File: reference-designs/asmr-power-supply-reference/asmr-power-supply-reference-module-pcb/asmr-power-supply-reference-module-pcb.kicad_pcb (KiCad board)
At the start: 2 copper layers, 136 x 72 mm, 74 parts, among them J2 USB_C_Receptacle_USB2.0_14P, J3 PWR-SW, Q1 DMP3036SFV, U1 HUSB238, U2 MP2328C, U3 MCP1365, U4 MP2328C

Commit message: More changes to DreamLand.
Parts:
- Q1: footprint Package_SON:VSON-8_3.3x3.3mm_P0.65mm_NexFET -> CM_Chip_Packages:VSON-8_3.3x3.3mm_P0.65mm_NexFET
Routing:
- net +20V: track 58.4 -> 53.3 mm

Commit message: Tune final power supply design.
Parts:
- J3: footprint Connector_JST:JST_SH_BM02B-SRSS-TB_1x02-1MP_P1.00mm_Vertical -> CM_Connector_JST:JST_SH_BM02B-SRSS-TB_1x02-1MP_P1.00mm_Vertical
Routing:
- net Net-(J3-Pin_2): track 9.48 -> 10.2 mm
- net GND_CH: vias 298 -> 299
- net /Vbus: vias 0 -> 1
- net -15V: vias 6 -> 7
- net +5V: vias 6 -> 7
- net +20V: vias 4 -> 5
- net +15V: vias 6 -> 7
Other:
- outline, holes or cut-outs redrawn
- board text added: "ABSOLUTELY"
- board text added: "ASMR"
- board text added: "Advanced Synth Module Rack"
- board text added: "Do NOT attempt to use in a computer."
- board text added: "NOT PCI !"
- board text added: "Power Switch"
- board text added: "Reference Power Supply"
- board text added: "Rev. A (2025/09)"
- board text added: "SMOKE, FIRE OR SMELLS MAY OCCUR."
- board text added: "by Circuit Monkey"
- board text added: "for"

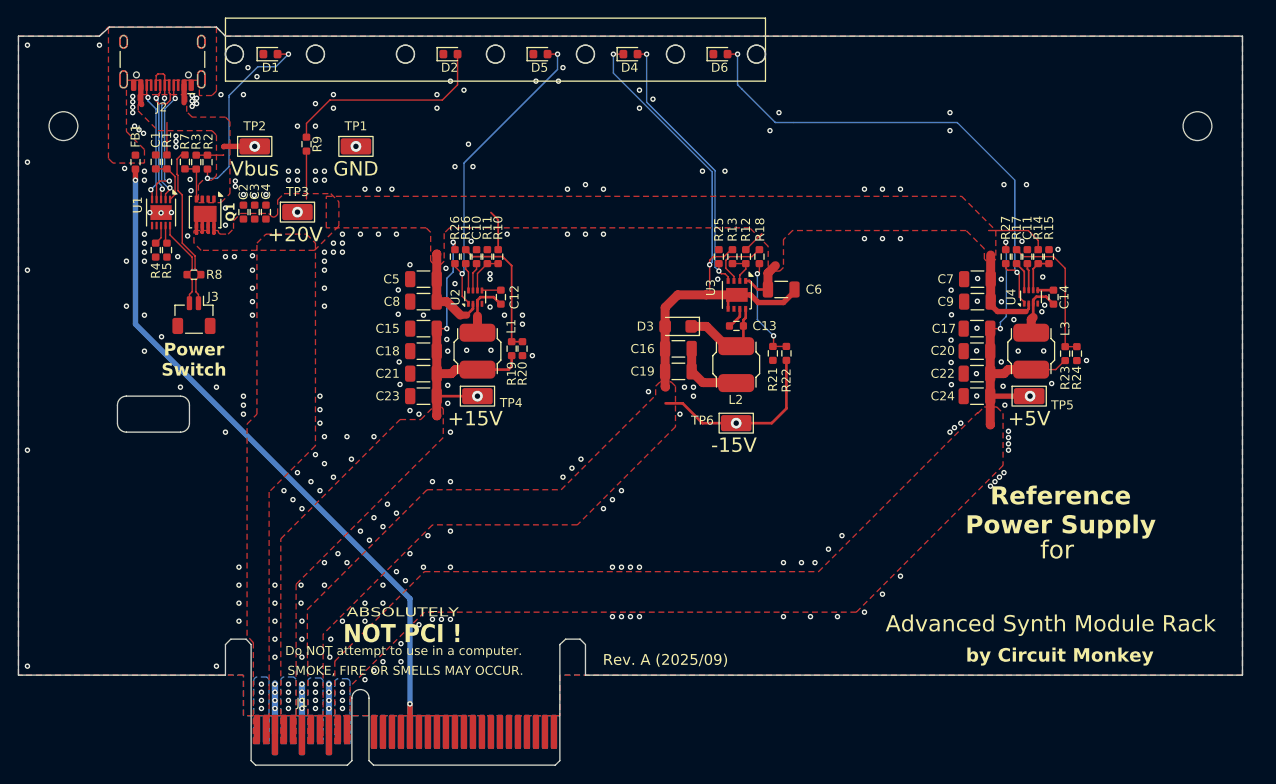
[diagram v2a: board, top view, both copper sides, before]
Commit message: Final tuning for power supply.
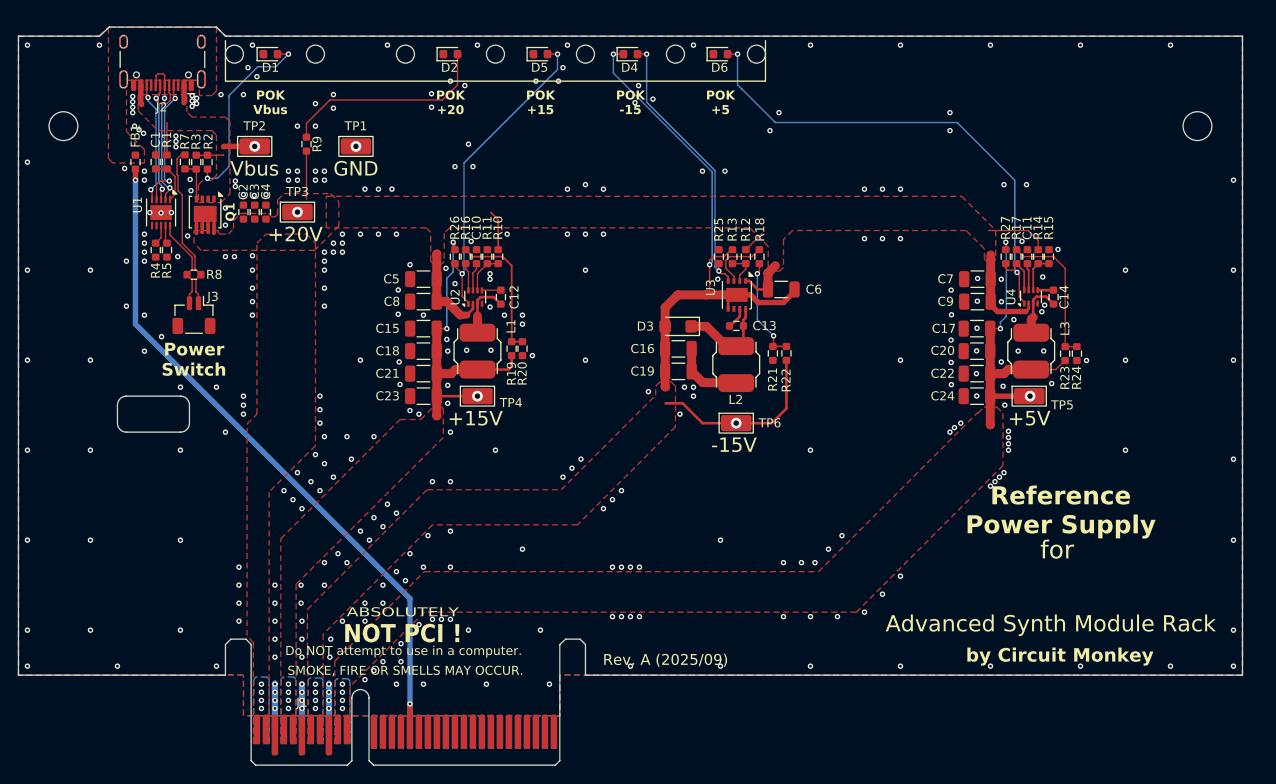
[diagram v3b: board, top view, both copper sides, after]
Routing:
- net GND_CH: vias 299 -> 352
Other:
- board text added: "POK +15"
- board text added: "POK +20"
- board text added: "POK +5"
- board text added: "POK -15"
- board text added: "POK Vbus"
